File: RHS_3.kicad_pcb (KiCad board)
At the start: 2 copper layers, 51 x 61 mm, 37 parts, among them IC1 ATMEGA328P-A, IC2 CC1101, J1 Glass Breakage Detector, J2 ANT, P4 ISP Bottom, P5 ISP Top, P6 FTDI, P7 ISP 10, SW1 Reset, SW2 Config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

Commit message: fix missing GND
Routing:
- net GND: track 65.3 -> 67.9 mm
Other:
- board text added: "RHS-3 V1.2"
- board text removed: "RHS-3 V1.1"
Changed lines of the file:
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@@
     (thickness 1.6)
     (drawings 33)
-    (tracks 477)
+    (tracks 481)
     (zones 0)
     (modules 37)
@@
     (effects (font (size 1 1) (thickness 0.2)))
   )
-  (gr_text "RHS-3\nV1.1" (at 88.519 119.888 90) (layer F.SilkS)
+  (gr_text "RHS-3\nV1.2" (at 88.519 119.888 90) (layer F.SilkS)
     (effects (font (size 1.5 1.5) (thickness 0.3)))
   )
@@
   (via (at 81.26 125.46) (size 0.8) (drill 0.4) (layers F.Cu B.Cu) (net 2))
   (via (at 90.95 125.54) (size 0.8) (drill 0.4) (layers F.Cu B.Cu) (net 2))
+  (segment (start 101.1 87.25) (end 101.482 86.868) (width 0.25) (layer B.Cu) (net 2))
+  (segment (start 101.1 88) (end 101.1 87.25) (width 0.25) (layer B.Cu) (net 2))
+  (segment (start 101.489 86.875) (end 102.86 86.875) (width 0.25) (layer B.Cu) (net 2))
+  (segment (start 101.482 86.868) (end 101.489 86.875) (width 0.25) (layer B.Cu) (net 2))
   (via (at 64.03 98.97) (size 0.8) (drill 0.4) (layers F.Cu B.Cu) (net 3))
   (segment (start 64.435 98.97) (end 64.03 98.97) (width 0.25) (layer B.Cu) (net 3))
@@
     (connect_pads (clearance 0.508))
     (min_thickness 0.254)
-    (fill yes (arc_segments 32) (thermal_gap 0.508) (thermal_bridge_width 0.508))
+    (fill (arc_segments 32) (thermal_gap 0.508) (thermal_bridge_width 0.508))
     (polygon
       (pts
@@
     (connect_pads (clearance 0.508))
     (min_thickness 0.254)
-    (fill yes (arc_segments 32) (thermal_gap 0.508) (thermal_bridge_width 0.508))
+    (fill (arc_segments 32) (thermal_gap 0.508) (thermal_bridge_width 0.508))
     (polygon
       (pts

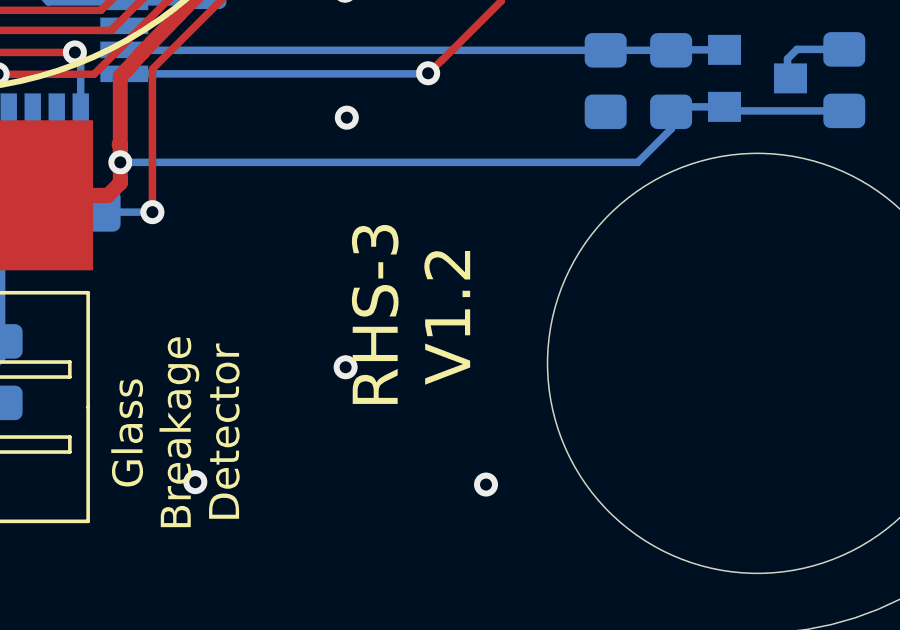
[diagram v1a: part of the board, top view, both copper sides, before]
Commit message: fix missing GND areas
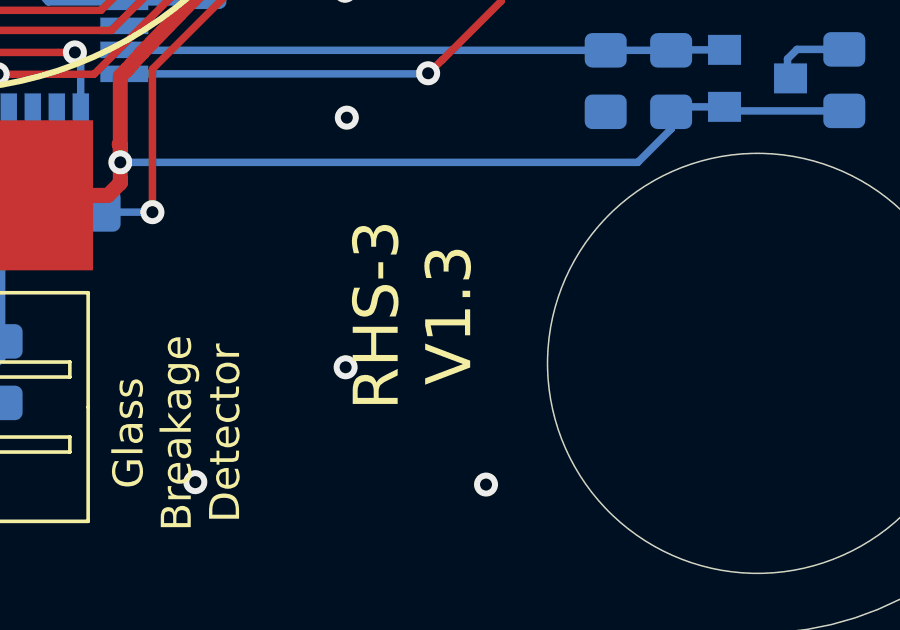
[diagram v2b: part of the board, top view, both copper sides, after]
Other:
- board text added: "RHS-3 V1.3"
- board text removed: "RHS-3 V1.2"
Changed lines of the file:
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@@
     (effects (font (size 1 1) (thickness 0.2)))
   )
-  (gr_text "RHS-3\nV1.2" (at 88.519 119.888 90) (layer F.SilkS)
+  (gr_text "RHS-3\nV1.3" (at 88.519 119.888 90) (layer F.SilkS)
     (effects (font (size 1.5 1.5) (thickness 0.3)))
   )
@@
     (connect_pads (clearance 0.508))
     (min_thickness 0.254)
-    (fill (arc_segments 32) (thermal_gap 0.508) (thermal_bridge_width 0.508))
+    (fill yes (arc_segments 32) (thermal_gap 0.508) (thermal_bridge_width 0.508))
     (polygon
       (pts
@@
     (connect_pads (clearance 0.508))
     (min_thickness 0.254)
-    (fill (arc_segments 32) (thermal_gap 0.508) (thermal_bridge_width 0.508))
+    (fill yes (arc_segments 32) (thermal_gap 0.508) (thermal_bridge_width 0.508))
     (polygon
       (pts

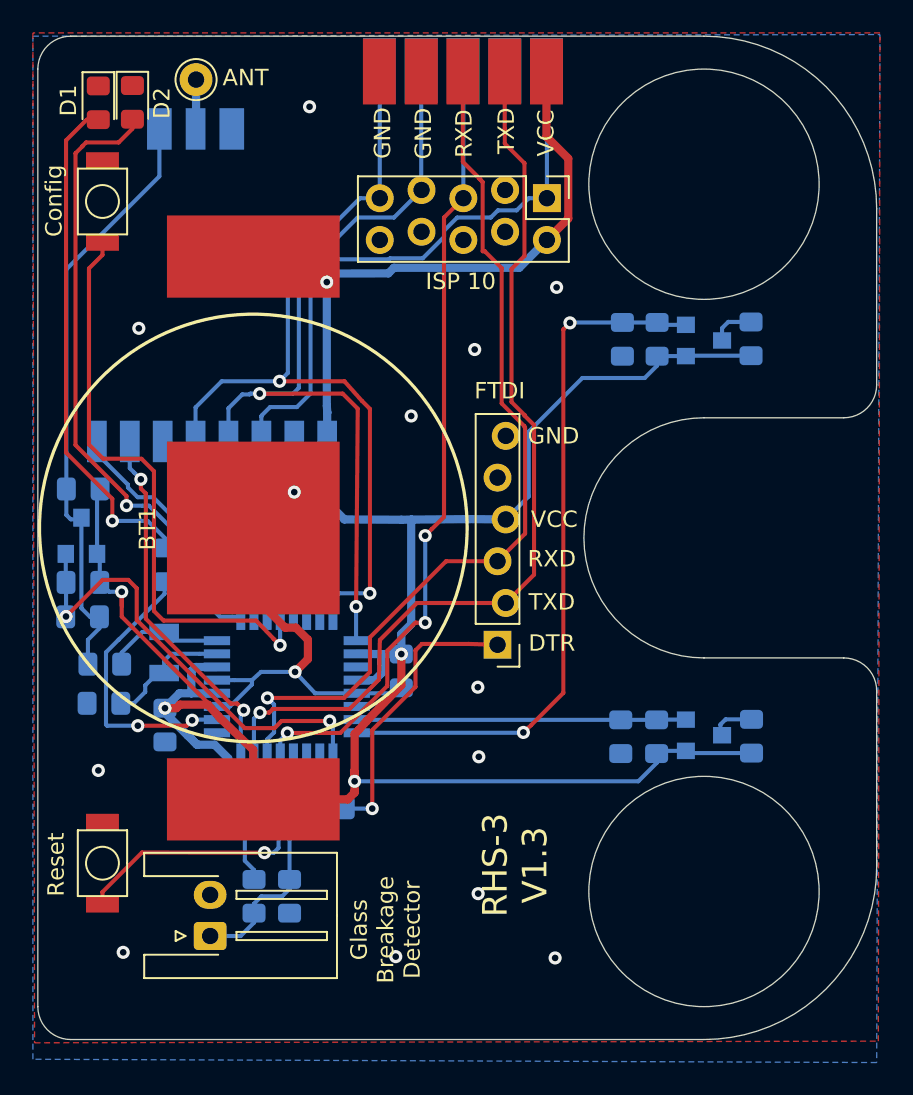
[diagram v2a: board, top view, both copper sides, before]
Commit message: optional CC1101 direct use
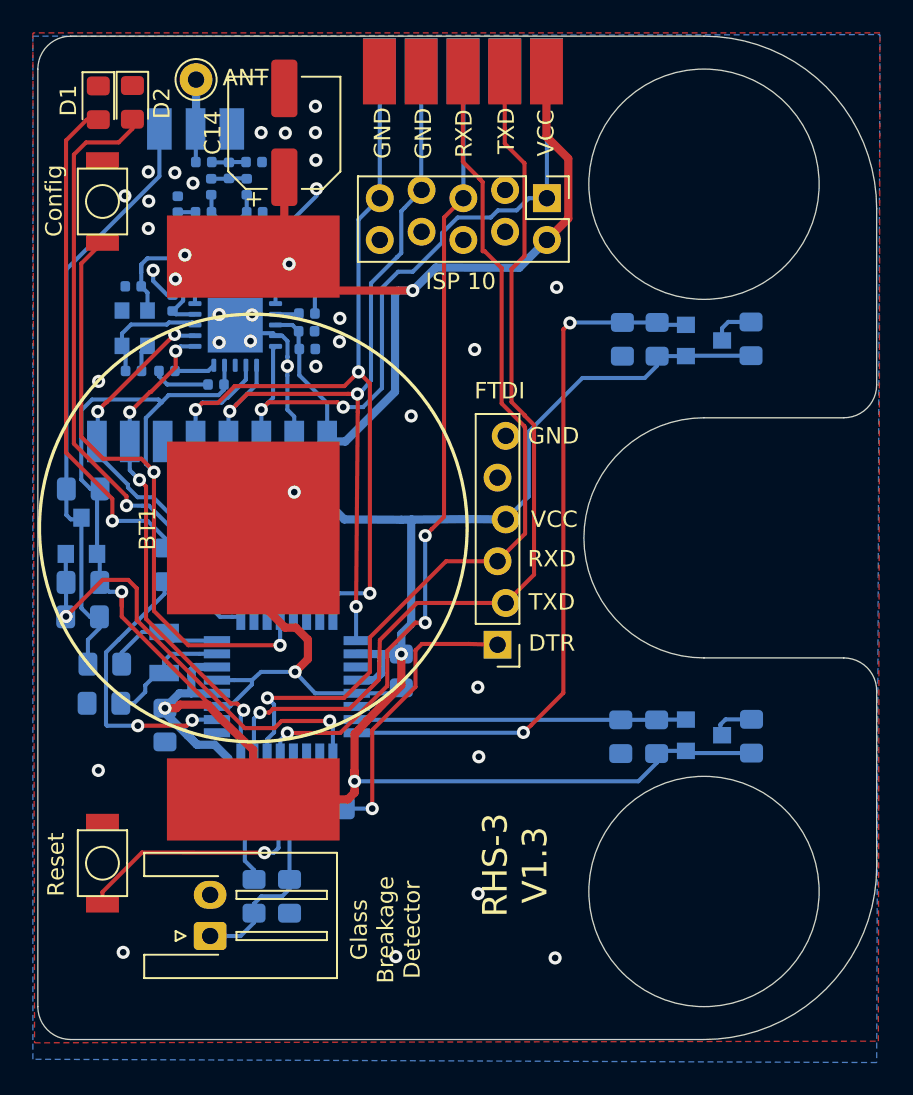
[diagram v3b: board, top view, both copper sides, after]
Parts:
- added C14: 330µ, Capacitor_SMD:CP_Elec_6.3x5.8, F.Cu at (74.5, 75.4)
- added C15: 4u7, Capacitor_SMD:C_0402_1005Metric, B.Cu at (75.9, 88.5)
- added C16: 100n, Capacitor_SMD:C_0402_1005Metric, B.Cu at (72.8, 82.8)
- added C17: 100n, Capacitor_SMD:C_0402_1005Metric, B.Cu at (75.8, 87.4)
- added C18: 100n, Capacitor_SMD:C_0402_1005Metric, B.Cu at (73.9, 82.8)
- added C19: 100n, Capacitor_SMD:C_0402_1005Metric, B.Cu at (69.5, 82.8)
- added C20: 100n, Capacitor_SMD:C_0402_1005Metric, B.Cu at (70.3, 90.7)
- added C21: 100n, Capacitor_SMD:C_0402_1005Metric, B.Cu at (67.7, 85.7)
- added C22: 100n, Capacitor_SMD:C_0402_1005Metric, B.Cu at (67.4, 89.9)
- added C23: 12p, Capacitor_SMD:C_0402_1005Metric, B.Cu at (65.3, 89.9)
- added C24: 15p, Capacitor_SMD:C_0402_1005Metric, B.Cu at (65.3, 84.7)
- added C25: 1p5, Capacitor_SMD:C_0402_1005Metric, B.Cu at (72.7, 80.2)
- added C26: 1p, Capacitor_SMD:C_0402_1005Metric, B.Cu at (71.1, 81.3)
- added C27: 1p5, Capacitor_SMD:C_0402_1005Metric, B.Cu at (68.0, 79.7)
- added C28: 1p5, Capacitor_SMD:C_0402_1005Metric, B.Cu at (70.0, 78.7)
- added C29: 3p3, Capacitor_SMD:C_0402_1005Metric, B.Cu at (72.6, 77.2)
- added IC3: CC1101_Chip, Package_DFN_QFN:QFN-20-1EP_5x5mm_P0.65mm_EP3.35x3.35mm, B.Cu at (71.5, 87.1)
- added L1: 12nH, Inductor_SMD:L_0402_1005Metric, B.Cu at (71.7, 82.8)
- added L2: 12nH, Inductor_SMD:L_0402_1005Metric, B.Cu at (70.5, 82.9)
- added L3: 18nH, Inductor_SMD:L_0402_1005Metric, B.Cu at (69.6, 80.2)
- added L4: 18nH, Inductor_SMD:L_0402_1005Metric, B.Cu at (72.2, 78.7)
- added L5: 12nH, Inductor_SMD:L_0402_1005Metric, B.Cu at (71.1, 77.7)
- added L6: 12nH, Inductor_SMD:L_0402_1005Metric, B.Cu at (69.6, 77.2)
- added R8: 56k, Resistor_SMD:R_0402_1005Metric, B.Cu at (75.9, 86.4)
- added X1: Resonator, Oscillator:Oscillator_SMD_EuroQuartz_XO32-4Pin_3.2x2.5mm, B.Cu at (65.4, 87.3)
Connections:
- net Net-(IC1-Pad14) renamed /CS
- net Net-(IC1-Pad32) renamed /GDO0
- net Net-(IC2-Pad9) renamed /ANT
- IC1 pad 12: Net-(IC1-Pad12) -> VCC
- SW2 pad 1: Net-(IC1-Pad12) -> VCC
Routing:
- net VCC: track 189.5 -> 282.1 mm, vias 5 -> 10
- net Net-(IC1-Pad12): track 36.0 -> 0.00 mm, vias 1 -> 0
- net GND: track 67.9 -> 97.4 mm, vias 14 -> 34
- net /CS: track 19.9 -> 29.7 mm, vias 0 -> 2
- net Net-(C24-Pad1): track 0.00 -> 8.78 mm
- net /GDO0: track 22.3 -> 30.3 mm, vias 2 -> 4
- net Net-(C23-Pad1): track 0.00 -> 7.14 mm
- net /MOSI: track 53.3 -> 57.5 mm, vias 0 -> 2
- net Net-(C26-Pad2): track 0.00 -> 3.55 mm
- net Net-(C25-Pad2): track 0.00 -> 3.48 mm
- net /MISO: track 50.8 -> 53.5 mm, vias 2 -> 3
- net Net-(C22-Pad1): track 0.00 -> 2.51 mm
- net Net-(C28-Pad1): track 0.00 -> 2.18 mm
- net Net-(C29-Pad1): track 0.00 -> 2.10 mm
- net /ANT: track 6.06 -> 8.08 mm
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
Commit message: Jumper added to prepare switch of VCC for CC1101 und Sensors
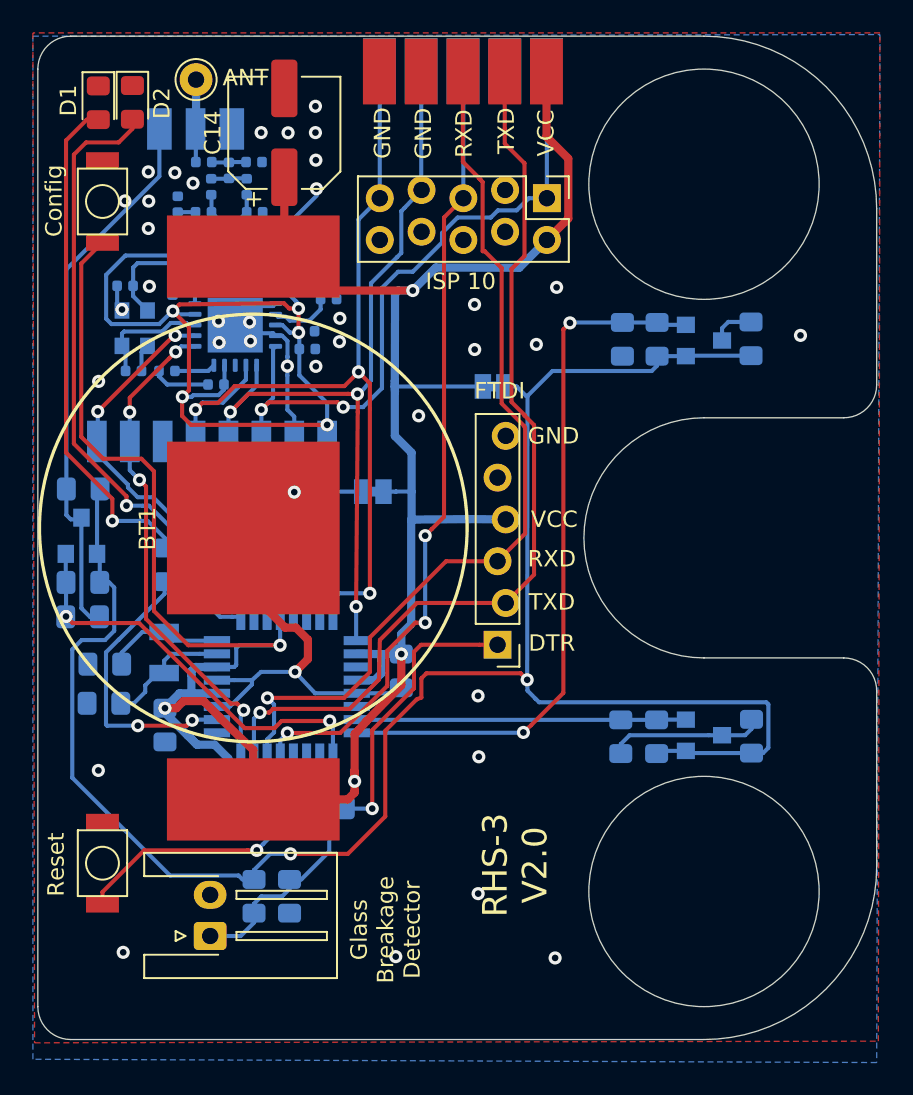
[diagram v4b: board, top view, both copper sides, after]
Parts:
- added JP1: Jumper_NO_Small, Jumper:SolderJumper-2_P1.3mm_Bridged_Pad1.0x1.5mm, B.Cu at (79.9, 97.2)
- added JP2: Jumper_NO_Small, Jumper:SolderJumper-2_P1.3mm_Bridged_Pad1.0x1.5mm, B.Cu at (87.2, 90.8)
- moved R8 1.58 mm to (77.2, 85.5)
- moved C24 0.50 mm to (64.8, 84.7)
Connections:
- C15 pad 1: VCC -> VSS
- C16 pad 1: VCC -> VSS
- C17 pad 1: VCC -> VSS
- C18 pad 1: VCC -> VSS
- C19 pad 1: VCC -> VSS
- C20 pad 1: VCC -> VSS
- C21 pad 1: VCC -> VSS
- C3 pad 1: VCC -> VSS
- C4 pad 1: VCC -> VDD
- C5 pad 1: VCC -> VDD
- C6 pad 1: VCC -> VDD
- IC2 pad 1: VCC -> VSS
- IC3 pad 11: VCC -> VSS
- IC3 pad 14: VCC -> VSS
- IC3 pad 15: VCC -> VSS
- IC3 pad 18: VCC -> VSS
- IC3 pad 4: VCC -> VSS
- IC3 pad 9: VCC -> VSS
- R4 pad 1: VCC -> VDD
- R5 pad 1: VCC -> VDD
- R6 pad 1: VCC -> VDD
- R7 pad 1: VCC -> VDD
- U1 pad 1: VCC -> VDD
- U2 pad 1: VCC -> VDD
- U3 pad 1: VCC -> VDD
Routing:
- net VDD: track 0.00 -> 119.1 mm, vias 0 -> 2
- net VCC: track 282.1 -> 176.5 mm, vias 10 -> 5
- net VSS: track 0.00 -> 68.5 mm, vias 0 -> 5
- net /A2: track 28.2 -> 25.2 mm
- net Net-(IC3-Pad17): track 1.44 -> 3.81 mm
- net GND: track 97.4 -> 98.1 mm, vias 34 -> 38
- net /RESET: track 68.7 -> 68.0 mm
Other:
- board text added: "RHS-3 V2.0"
- board text removed: "RHS-3 V1.3"

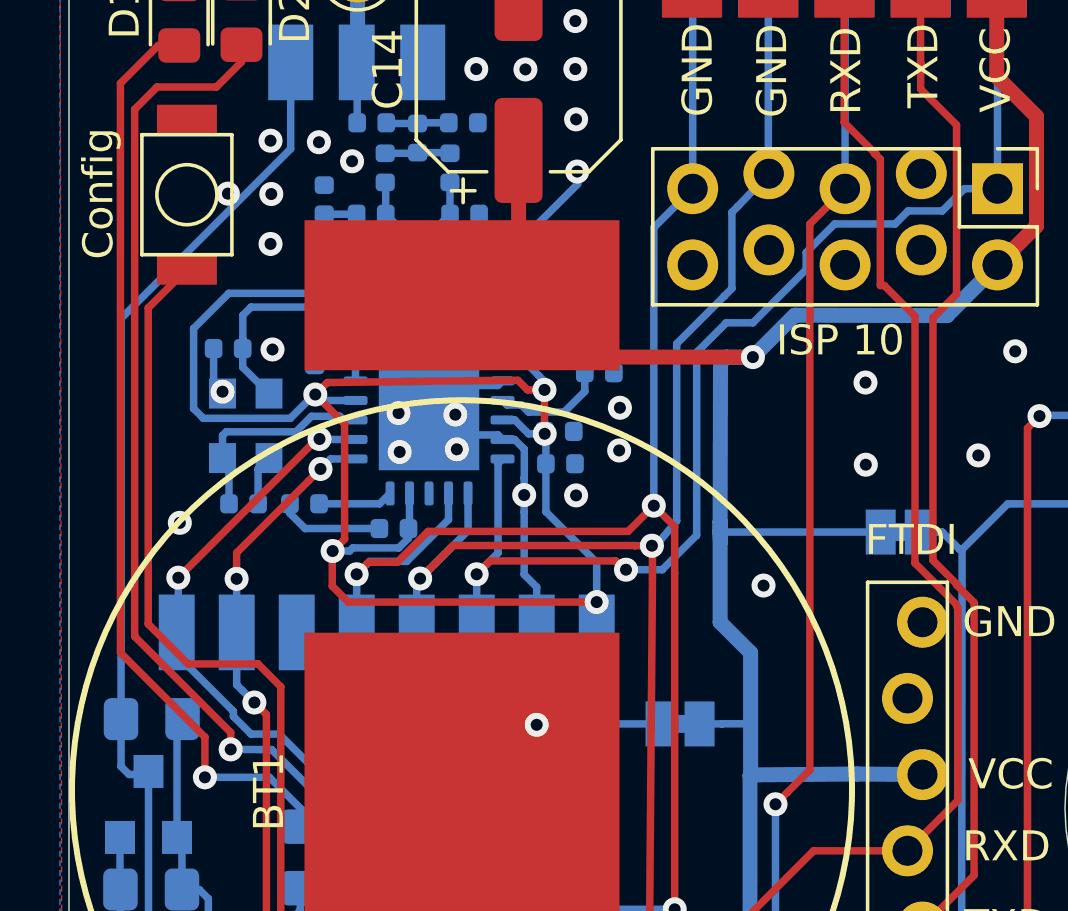
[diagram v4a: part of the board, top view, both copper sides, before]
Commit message: CC1101 footprint fixed
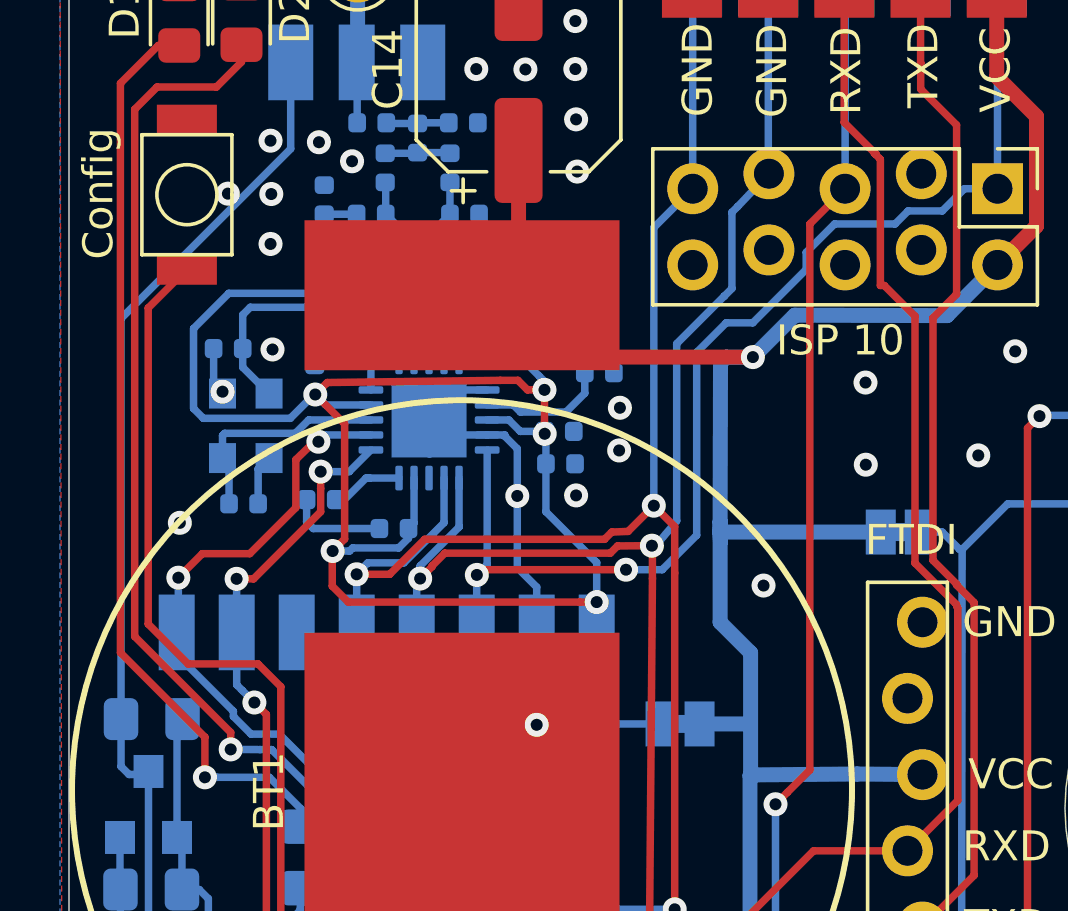
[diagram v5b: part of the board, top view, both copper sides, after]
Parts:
- IC3: footprint Package_DFN_QFN:QFN-20-1EP_5x5mm_P0.65mm_EP3.35x3.35mm -> Package_DFN_QFN:QFN-20-1EP_4x4mm_P0.5mm_EP2.5x2.5mm
- moved C22 0.57 mm to (67.9, 89.7)
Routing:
- net GND: track 98.1 -> 90.3 mm, vias 38 -> 34
- net VSS: track 68.5 -> 72.1 mm
- net /CS: track 29.5 -> 31.1 mm
- net /GDO0: track 30.2 -> 31.2 mm
- net Net-(IC3-Pad12): track 1.38 -> 1.96 mm
- net Net-(C24-Pad1): track 8.90 -> 9.45 mm
- net Net-(IC3-Pad13): track 1.36 -> 1.87 mm
